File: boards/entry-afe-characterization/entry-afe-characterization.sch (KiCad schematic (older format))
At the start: 0 parts

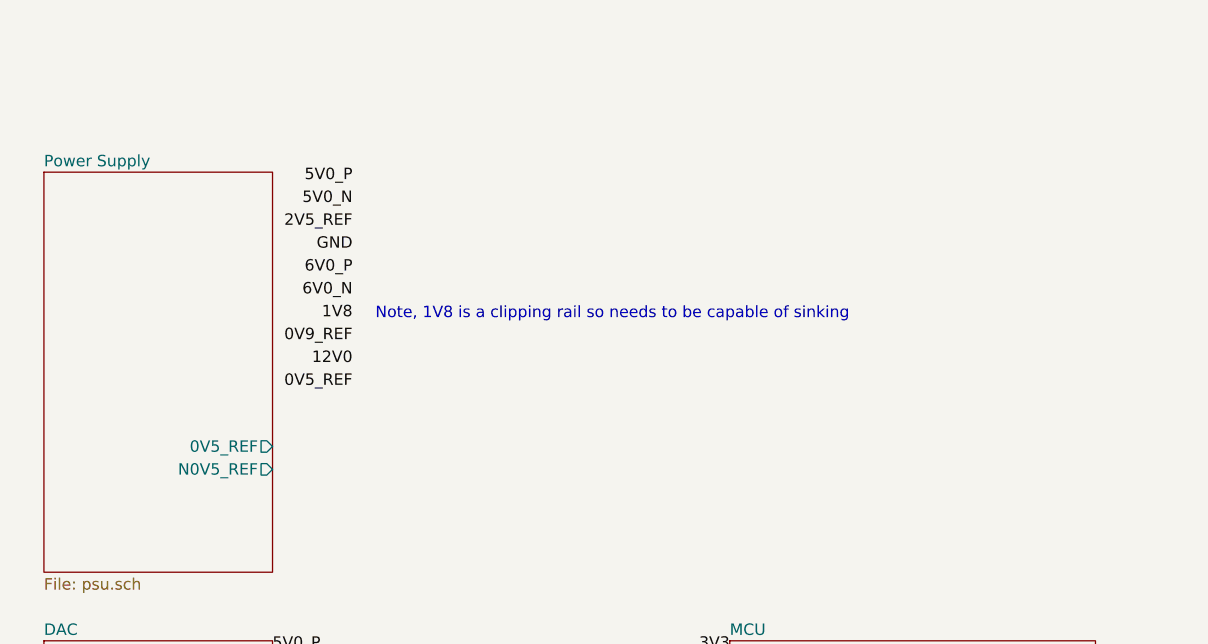
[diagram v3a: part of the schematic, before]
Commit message: Updated entry-afe-characterization with progress on power supply
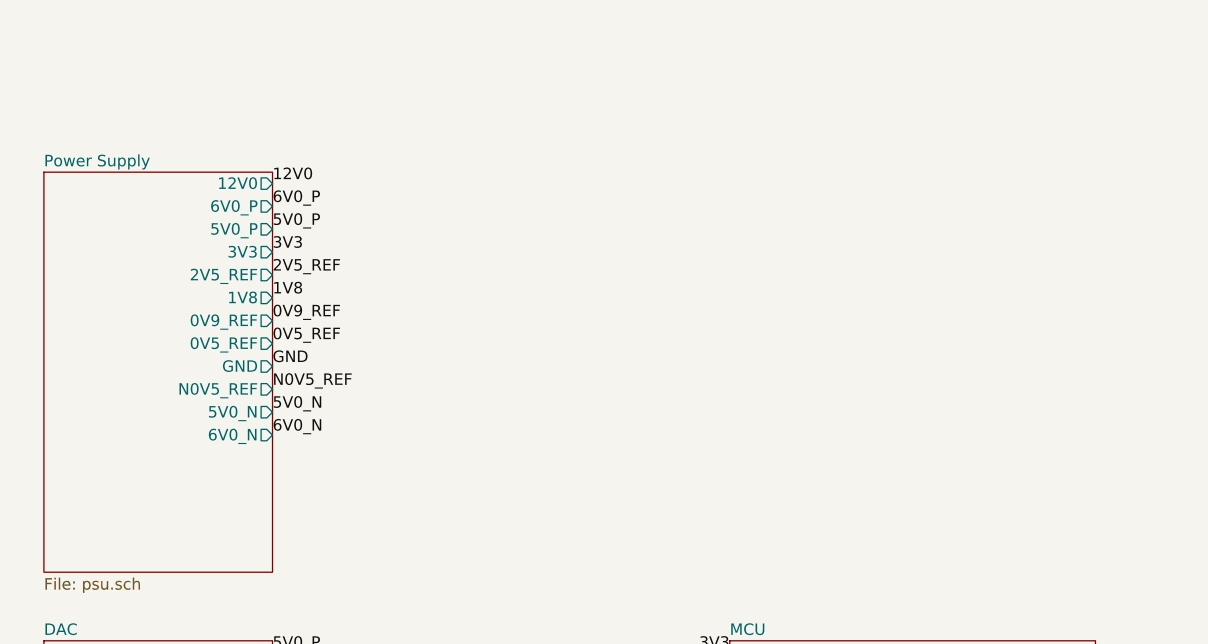
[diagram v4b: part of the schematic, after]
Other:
- note removed: "Note, 1V8 is a clipping rail so needs to be capable of sinking"
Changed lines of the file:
@@
 Sheet 1 8
 Title "Entry-Level Oscilloscope AFE Characterization Platform"
-Date "2020-03-24"
+Date "2020-03-26"
 Rev "0.1"
 Comp "Antikernel Labs"
@@
 F0 "Power Supply" 50
 F1 "psu.sch" 50
-F2 "0V5_REF" O R 2150 4750 50
-F3 "N0V5_REF" O R 2150 4850 50
+F2 "0V5_REF" O R 2150 4300 50
+F3 "N0V5_REF" O R 2150 4500 50
+F4 "5V0_P" O R 2150 3800 50
+F5 "5V0_N" O R 2150 4600 50
+F6 "12V0" O R 2150 3600 50
+F7 "GND" O R 2150 4400 50
+F8 "6V0_P" O R 2150 3700 50
+F9 "6V0_N" O R 2150 4700 50
+F10 "3V3" O R 2150 3900 50
+F11 "2V5_REF" O R 2150 4000 50
+F12 "1V8" O R 2150 4100 50
+F13 "0V9_REF" O R 2150 4200 50
 $EndSheet
 Text Notes 6300 4350 0    50   ~ 0
@@
 Text Label 2150 6750 0    50   ~ 0
 VIN_OFFSET
-Text Label 2500 3600 2    50   ~ 0
-5V0_P
-Text Label 2500 3700 2    50   ~ 0
-5V0_N
-Text Label 2500 3900 2    50   ~ 0
-GND
-Text Label 2500 3800 2    50   ~ 0
+Text Label 2150 3800 0    50   ~ 0
+5V0_P
+Text Label 2150 4600 0    50   ~ 0
+5V0_N
+Text Label 2150 4400 0    50   ~ 0
+GND
+Text Label 2150 4000 0    50   ~ 0
 2V5_REF
 Text Notes 1150 2700 0    50   ~ 0
@@
 F3 "VGAIN_N" I L 6600 850 50
 F4 "GND" I L 6600 1350 50
-F7 "0V9_REF" I L 6600 1250 50
-F8 "5V0_P" I L 6600 1050 50
-F9 "5V0_N" I L 6600 1450 50
-F10 "1V8" I L 6600 1150 50
+F5 "0V9_REF" I L 6600 1250 50
+F6 "5V0_P" I L 6600 1050 50
+F7 "5V0_N" I L 6600 1450 50
+F8 "1V8" I L 6600 1150 50
 $EndSheet
 Wire Wire Line
@@
 Text Label 2850 1150 2    50   ~ 0
 6V0_N
-Text Label 2500 4000 2    50   ~ 0
+Text Label 2150 3700 0    50   ~ 0
 6V0_P
-Text Label 2500 4100 2    50   ~ 0
+Text Label 2150 4700 0    50   ~ 0
 6V0_N
-Text Label 2500 4300 2    50   ~ 0
+Text Label 2150 4200 0    50   ~ 0
 0V9_REF
 Text Label 1150 850  2    50   ~ 0
@@
 Text Label 1150 750  2    50   ~ 0
 12V0
-Text Label 2500 4400 2    50   ~ 0
+Text Label 2150 3600 0    50   ~ 0
 12V0
-Text Label 2500 4500 2    50   ~ 0
+Text Label 2150 4300 0    50   ~ 0
 0V5_REF
 Text Label 1150 1150 2    50   ~ 0
@@
 Text Label 6600 1450 2    50   ~ 0
 5V0_N
-Text Label 2500 4200 2    50   ~ 0
+Text Label 2150 4100 0    50   ~ 0
 1V8
-Text Notes 2600 4200 0    50   ~ 0
-Note, 1V8 is a clipping rail so needs to be capable of sinking
 $Sheet
 S 1150 5600 1000 1750
@@
 Text Label 5750 6150 0    50   ~ 0
 INPUT_RST
+Text Label 2150 3900 0    50   ~ 0
+3V3
+Text Label 2150 4500 0    50   ~ 0
+N0V5_REF
 $EndSCHEMATC

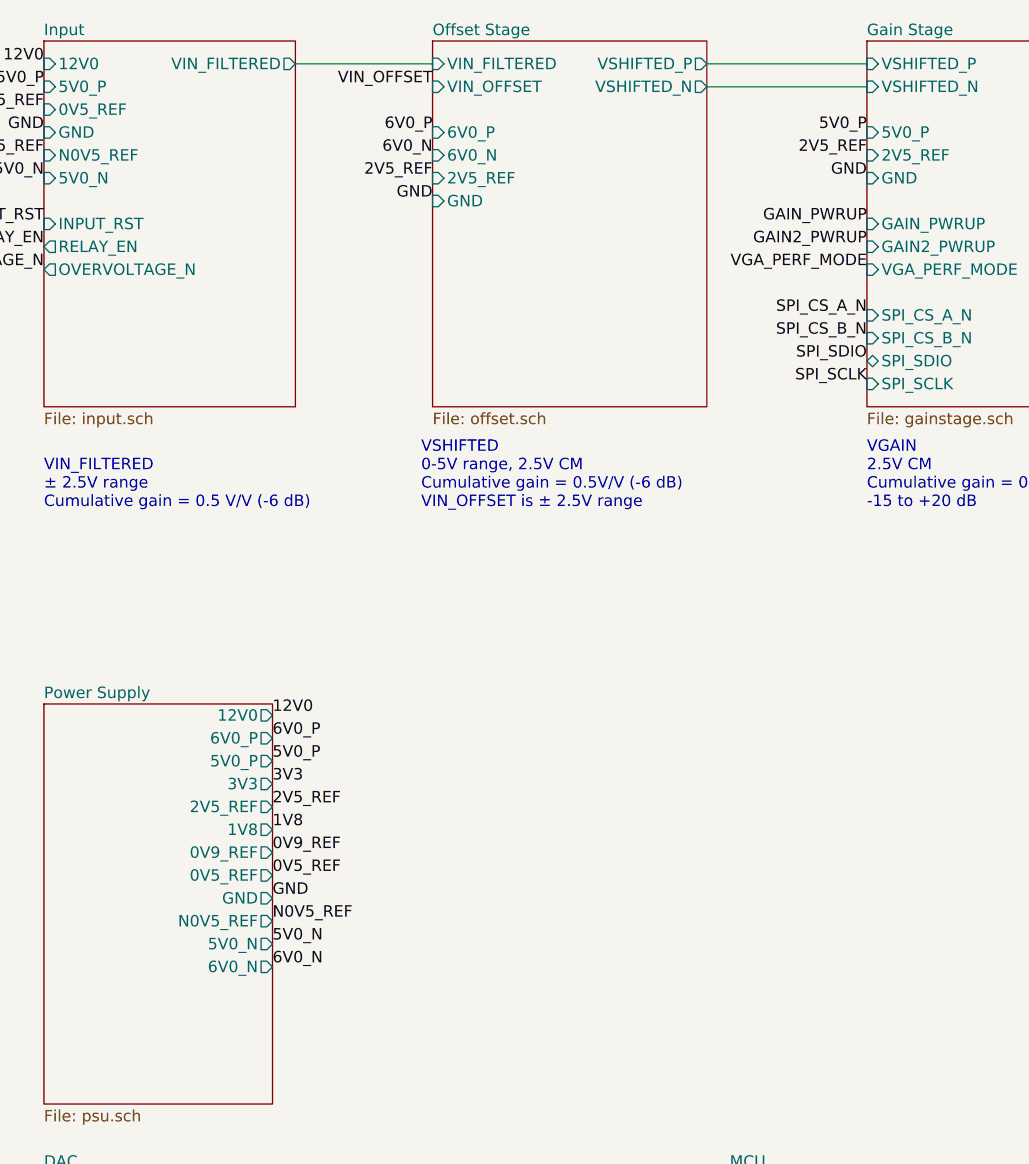
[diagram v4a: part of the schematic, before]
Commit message: Continued design review, added U18 to offset stage
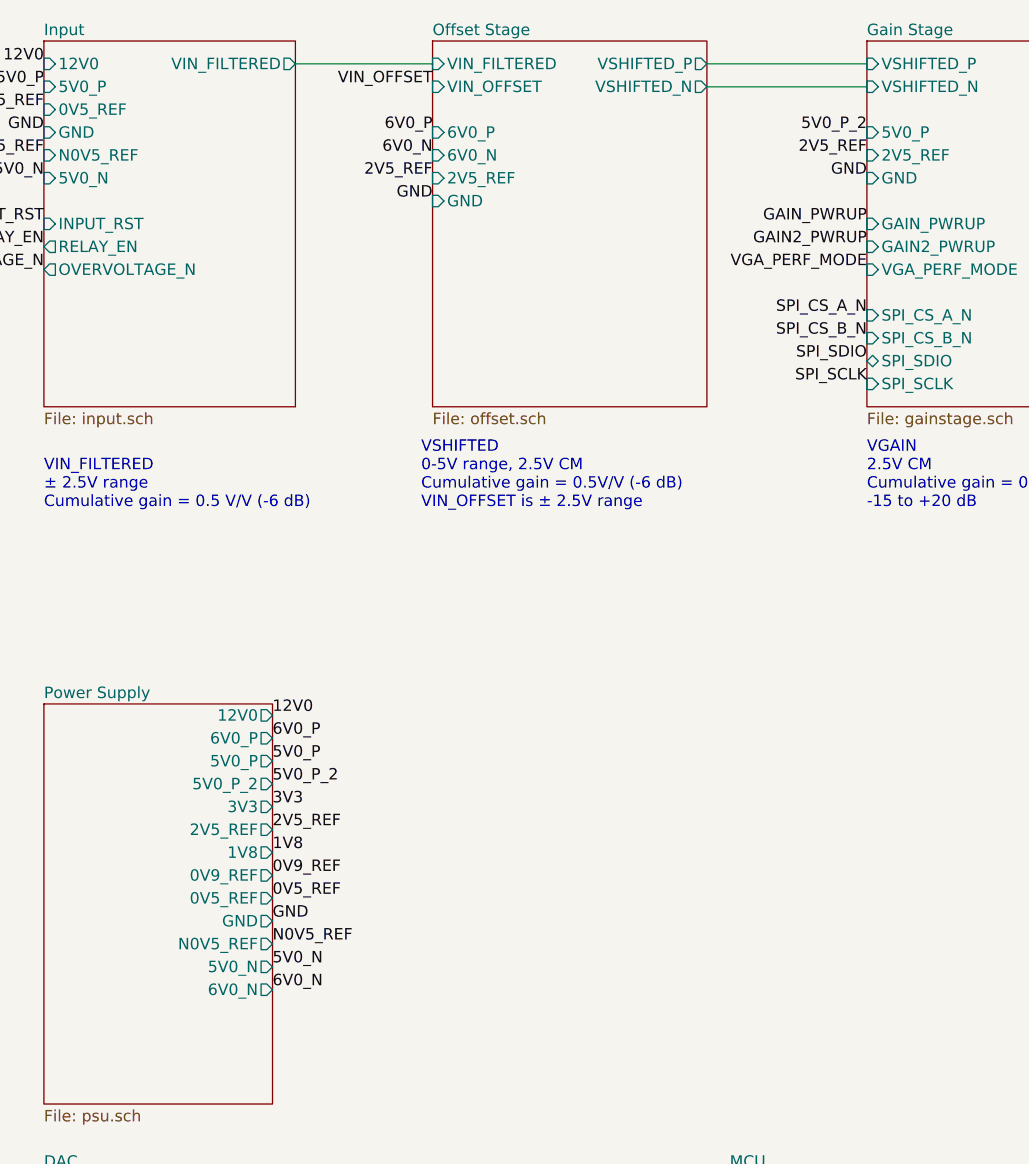
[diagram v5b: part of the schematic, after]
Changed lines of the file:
@@
 Sheet 1 8
 Title "Entry-Level Oscilloscope AFE Characterization Platform"
-Date "2020-03-26"
+Date "2020-03-27"
 Rev "0.1"
 Comp "Antikernel Labs"
@@
 Comment4 ""
 $EndDescr
-$Sheet
-S 1150 3550 1000 1750
-U 5E704852
-F0 "Power Supply" 50
-F1 "psu.sch" 50
-F2 "0V5_REF" O R 2150 4300 50
-F3 "N0V5_REF" O R 2150 4500 50
-F4 "5V0_P" O R 2150 3800 50
-F5 "5V0_N" O R 2150 4600 50
-F6 "12V0" O R 2150 3600 50
-F7 "GND" O R 2150 4400 50
-F8 "6V0_P" O R 2150 3700 50
-F9 "6V0_N" O R 2150 4700 50
-F10 "3V3" O R 2150 3900 50
-F11 "2V5_REF" O R 2150 4000 50
-F12 "1V8" O R 2150 4100 50
-F13 "0V9_REF" O R 2150 4200 50
-$EndSheet
 Text Notes 6300 4350 0    50   ~ 0
 SYSTEM GAIN CALCULATIONS\n\nHMCAD1520 wants 2V full scale\nIn 12-bit mode: 488 µV/LSB @ 0 dB gain\nIn 8-bit mode: 7.8 mV/LSB @ 0 dB gain\n\nMIN GAIN:\n10V input range, -13 dB system gain (0.2V/V)\n-9 dB gain on VGA\n12 bit mode: 2.4 mV/LSB\n8 bit mode: 39 mV/LSB\n\nMAX GAIN:\n159 mV input range, +22 dB system gain (12.59V/V)\n+26 dB gain on VGA\n12 bit mode: 38.7 µV/LSB\n8 bit mode: 619.5 µV/LSB
@@
 Text Label 2150 3800 0    50   ~ 0
 5V0_P
-Text Label 2150 4600 0    50   ~ 0
-5V0_N
-Text Label 2150 4400 0    50   ~ 0
-GND
-Text Label 2150 4000 0    50   ~ 0
+Text Label 2150 4700 0    50   ~ 0
+5V0_N
+Text Label 2150 4500 0    50   ~ 0
+GND
+Text Label 2150 4100 0    50   ~ 0
 2V5_REF
 Text Notes 1150 2700 0    50   ~ 0
@@
 Text Label 2150 3700 0    50   ~ 0
 6V0_P
-Text Label 2150 4700 0    50   ~ 0
+Text Label 2150 4800 0    50   ~ 0
 6V0_N
-Text Label 2150 4200 0    50   ~ 0
+Text Label 2150 4300 0    50   ~ 0
 0V9_REF
 Text Label 1150 850  2    50   ~ 0
@@
 Text Label 2150 3600 0    50   ~ 0
 12V0
-Text Label 2150 4300 0    50   ~ 0
+Text Label 2150 4400 0    50   ~ 0
 0V5_REF
 Text Label 1150 1150 2    50   ~ 0
@@
 GAIN2_PWRUP
 Text Label 4750 1050 2    50   ~ 0
-5V0_P
+5V0_P_2
 Text Label 4750 1250 2    50   ~ 0
 GND
@@
 Text Label 6600 1450 2    50   ~ 0
 5V0_N
-Text Label 2150 4100 0    50   ~ 0
+Text Label 2150 4200 0    50   ~ 0
 1V8
 $Sheet
@@
 Text Label 5750 6150 0    50   ~ 0
 INPUT_RST
+Text Label 2150 4000 0    50   ~ 0
+3V3
+Text Label 2150 4600 0    50   ~ 0
+N0V5_REF
+$Sheet
+S 1150 3550 1000 1750
+U 5E704852
+F0 "Power Supply" 50
+F1 "psu.sch" 50
+F2 "0V5_REF" O R 2150 4400 50
+F3 "N0V5_REF" O R 2150 4600 50
+F4 "5V0_P" O R 2150 3800 50
+F5 "5V0_N" O R 2150 4700 50
+F6 "12V0" O R 2150 3600 50
+F7 "GND" O R 2150 4500 50
+F8 "6V0_P" O R 2150 3700 50
+F9 "6V0_N" O R 2150 4800 50
+F10 "3V3" O R 2150 4000 50
+F11 "2V5_REF" O R 2150 4100 50
+F12 "1V8" O R 2150 4200 50
+F13 "0V9_REF" O R 2150 4300 50
+F14 "5V0_P_2" O R 2150 3900 50
+$EndSheet
 Text Label 2150 3900 0    50   ~ 0
-3V3
-Text Label 2150 4500 0    50   ~ 0
-N0V5_REF
+5V0_P_2
 $EndSCHEMATC

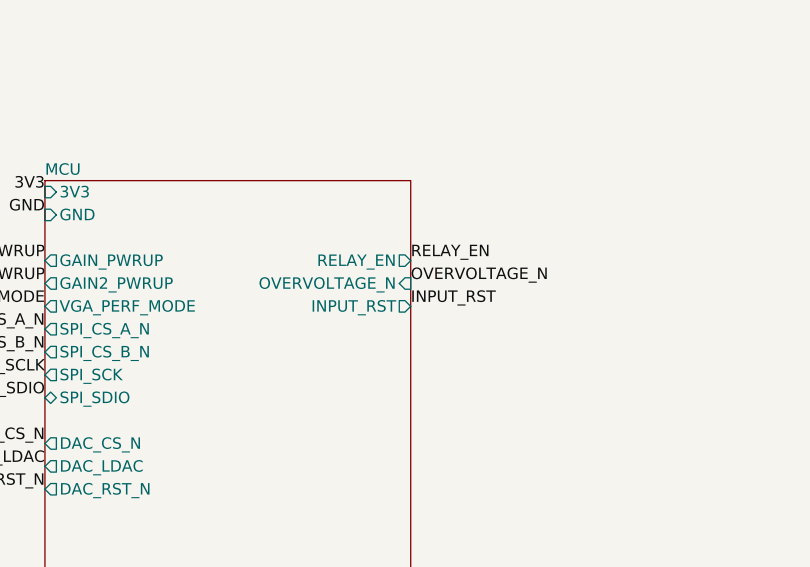
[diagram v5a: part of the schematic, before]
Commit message: Continued schematic review. Done with everything but test point/ground insertion.
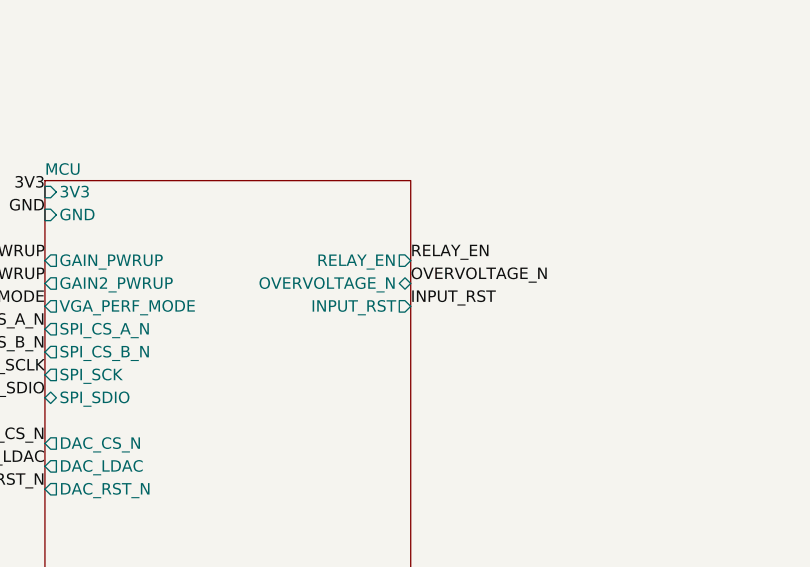
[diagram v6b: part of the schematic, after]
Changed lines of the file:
@@
 Sheet 1 8
 Title "Entry-Level Oscilloscope AFE Characterization Platform"
-Date "2020-03-27"
+Date "2020-03-28"
 Rev "0.1"
 Comp "Antikernel Labs"
@@
 F13 "DAC_RST_N" O L 4150 6950 50
 F14 "RELAY_EN" O R 5750 5950 50
-F15 "OVERVOLTAGE_N" I R 5750 6050 50
-F16 "INPUT_RST" O R 5750 6150 50
+F15 "INPUT_RST" O R 5750 6150 50
+F16 "OVERVOLTAGE_N" B R 5750 6050 50
 $EndSheet
 $Sheet
